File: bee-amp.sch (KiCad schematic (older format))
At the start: 35 parts, among them J1 Conn_01x02_Male, J10 Conn_01x02, J2 Conn_01x02_Male, J3 Conn_01x02_Male, J4 Conn_01x02_Male, J7 Conn_01x03, J8 Conn_01x02, J9 Conn_01x02, U1 OP07

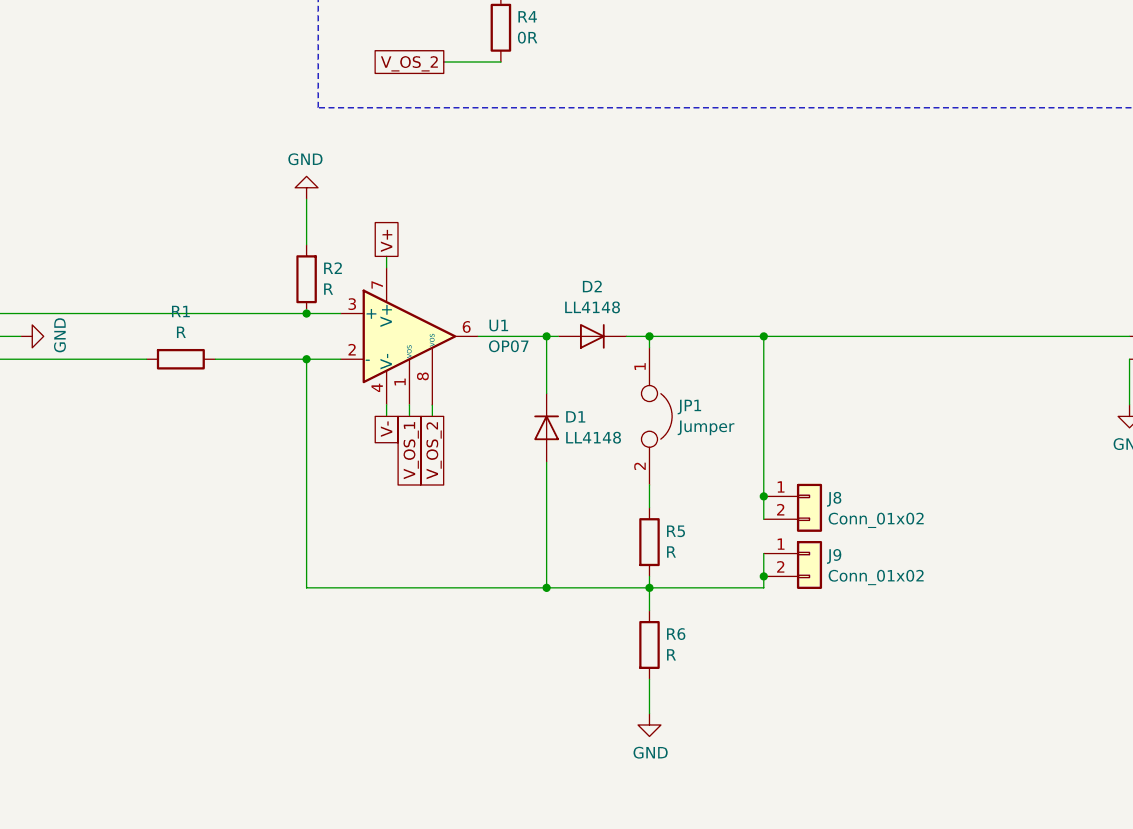
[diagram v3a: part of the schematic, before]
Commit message: Add part values, numbers and placement variants.
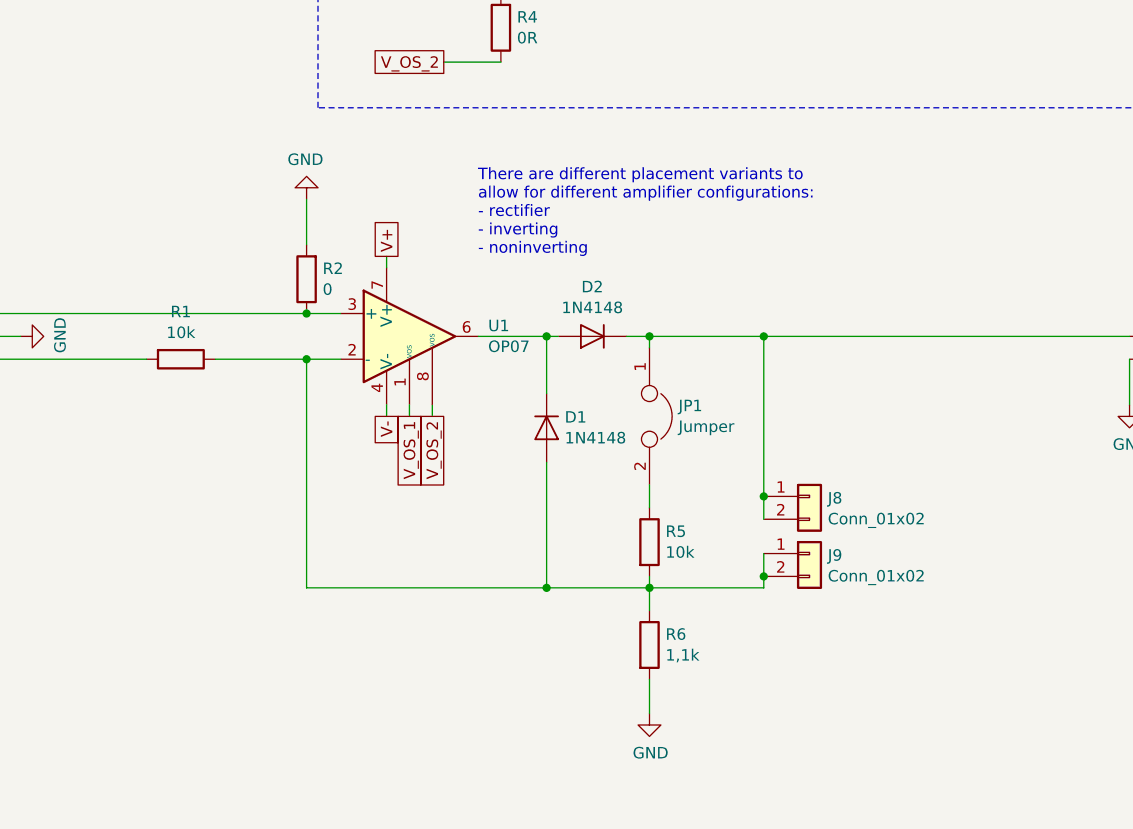
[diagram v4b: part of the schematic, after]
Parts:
- C1, C2: Reichelt Part No (none) -> X7R-G0805 100N; order number KEM X7R0805 100N -> (none)
- D1, D2: value LL4148 -> 1N4148; Reichelt Part No (none) -> 1N 4148 SMD; fit_field (none) -> +rectifier; order number 1N 4148 SMD -> (none)
- J1, J10, J2, J3, J4, JP1: Reichelt Part No (none) -> RND 205-00623
- J7: Reichelt Part No (none) -> RND 205-00624
- J8, J9: Reichelt Part No (none) -> MPE 006-1-002
- R1: value R -> 10k; Reichelt Part No (none) -> SMD-0805 10,0K; fit_field (none) -> +rectifier,+inverting
- R2: value R -> 0; Reichelt Part No (none) -> SMD-0805 0,00; fit_field (none) -> +rectifier,+inverting
- R3, R4: Reichelt Part No (none) -> RND 0805 1 0
- R5: value R -> 10k; Reichelt Part No (none) -> SMD-0805 10,0K
- R6: value R -> 1,1k; Reichelt Part No (none) -> RND 0805 1 1,1K; fit_field (none) -> +noninverting
- RV1: Reichelt Part No (none) -> 23A-20K; order number 23A-20K -> (none)
- U1: Reichelt Part No (none) -> OP 07 CD; order number OP 07 CD -> (none)
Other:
- note added: "There are different placement variants to \nallow for different amplifier configurations:\n- rectifier\n- inverting\n- noninverting"
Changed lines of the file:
@@
 F 2 "Connector_PinHeader_2.54mm:PinHeader_1x02_P2.54mm_Vertical" H 850 1300 50  0001 C CNN
 F 3 "~" H 850 1300 50  0001 C CNN
+F 4 "RND 205-00623" H 850 1300 50  0001 C CNN "Reichelt Part No"
 	1    850  1300
 	1    0    0    -1
@@
 F 2 "Connector_PinHeader_2.54mm:PinHeader_1x02_P2.54mm_Vertical" H 850 950 50  0001 C CNN
 F 3 "~" H 850 950 50  0001 C CNN
+F 4 "RND 205-00623" H 850 950 50  0001 C CNN "Reichelt Part No"
 	1    850  950
 	1    0    0    -1
@@
 F 2 "Connector_PinHeader_2.54mm:PinHeader_1x02_P2.54mm_Vertical" H 850 2150 50  0001 C CNN
 F 3 "~" H 850 2150 50  0001 C CNN
+F 4 "RND 205-00623" H 850 2150 50  0001 C CNN "Reichelt Part No"
 	1    850  2150
 	1    0    0    -1
@@
 F 2 "Connector_PinHeader_2.54mm:PinHeader_1x02_P2.54mm_Vertical" H 850 1800 50  0001 C CNN
 F 3 "~" H 850 1800 50  0001 C CNN
+F 4 "RND 205-00623" H 850 1800 50  0001 C CNN "Reichelt Part No"
 	1    850  1800
 	1    0    0    -1
@@
 F 2 "Package_SO:SO-8_5.3x6.2mm_P1.27mm" H 5550 3650 50  0001 C CNN
 F 3 "https://www.analog.com/media/en/technical-documentation/data-sheets/OP07.pdf" H 5550 3750 50  0001 C CNN
-F 4 "OP 07 CD" H 5500 3600 50  0001 C CNN "order number"
+F 4 "OP 07 CD" H 5500 3600 50  0001 C CNN "Reichelt Part No"
 	1    5500 3600
 	1    0    0    -1
@@
 F 2 "Connector_PinHeader_2.54mm:PinHeader_1x03_P2.54mm_Vertical" H 3400 3600 50  0001 C CNN
 F 3 "~" H 3400 3600 50  0001 C CNN
+F 4 "RND 205-00624" H 3400 3600 50  0001 C CNN "Reichelt Part No"
 	1    3400 3600
 	-1   0    0    -1
@@
 F 2 "Connector_PinHeader_2.54mm:PinHeader_1x02_P2.54mm_Vertical" H 8850 3600 50  0001 C CNN
 F 3 "~" H 8850 3600 50  0001 C CNN
+F 4 "RND 205-00623" H 8850 3600 50  0001 C CNN "Reichelt Part No"
 	1    8850 3600
 	1    0    0    -1
@@
 F 2 "Capacitor_SMD:C_0805_2012Metric_Pad1.15x1.40mm_HandSolder" H 2638 1050 50  0001 C CNN
 F 3 "https://www.reichelt.de/index.html?ACTION=7&LA=3&OPEN=0&INDEX=0&FILENAME=B300%252FKEM_C0XXX_X7R_DB-EN.pdf" H 2600 1200 50  0001 C CNN
-F 4 "KEM X7R0805 100N" H 2600 1200 50  0001 C CNN "order number"
+F 4 "X7R-G0805 100N" H 2600 1200 50  0001 C CNN "Reichelt Part No"
 	1    2600 1200
 	1    0    0    -1
@@
 P 4500 3700
 F 0 "R1" V 4293 3700 50  0000 C CNN
-F 1 "R" V 4384 3700 50  0000 C CNN
+F 1 "10k" V 4384 3700 50  0000 C CNN
 F 2 "Resistor_SMD:R_0805_2012Metric_Pad1.15x1.40mm_HandSolder" V 4430 3700 50  0001 C CNN
 F 3 "~" H 4500 3700 50  0001 C CNN
+F 4 "SMD-0805 10,0K" H 4500 3700 50  0001 C CNN "Reichelt Part No"
+F 5 "+rectifier,+inverting" H 4500 3700 50  0001 C CNN "fit_field"
 	1    4500 3700
 	0    1    1    0
@@
 P 6300 3600
 F 0 "D2" H 6300 3384 50  0000 C CNN
-F 1 "LL4148" H 6300 3475 50  0000 C CNN
+F 1 "1N4148" H 6300 3475 50  0000 C CNN
 F 2 "Diode_SMD:D_MiniMELF" H 6300 3425 50  0001 C CNN
 F 3 "http://www.vishay.com/docs/85557/ll4148.pdf" H 6300 3600 50  0001 C CNN
-F 4 "1N 4148 SMD" H 6300 3600 50  0001 C CNN "order number"
+F 4 "1N 4148 SMD" H 6300 3600 50  0001 C CNN "Reichelt Part No"
+F 5 "+rectifier" H 6300 3600 50  0001 C CNN "fit_field"
 	1    6300 3600
 	-1   0    0    1
@@
 F 2 "Capacitor_SMD:C_0805_2012Metric_Pad1.15x1.40mm_HandSolder" H 3688 1050 50  0001 C CNN
 F 3 "https://www.reichelt.de/index.html?ACTION=7&LA=3&OPEN=0&INDEX=0&FILENAME=B300%252FKEM_C0XXX_X7R_DB-EN.pdf" H 3650 1200 50  0001 C CNN
-F 4 "KEM X7R0805 100N" H 3650 1200 50  0001 C CNN "order number"
+F 4 "X7R-G0805 100N" H 3650 1200 50  0001 C CNN "Reichelt Part No"
 	1    3650 1200
 	1    0    0    -1
@@
 P 6550 4500
 F 0 "R5" H 6620 4546 50  0000 L CNN
-F 1 "R" H 6620 4455 50  0000 L CNN
+F 1 "10k" H 6620 4455 50  0000 L CNN
 F 2 "Resistor_SMD:R_0805_2012Metric_Pad1.15x1.40mm_HandSolder" V 6480 4500 50  0001 C CNN
 F 3 "~" H 6550 4500 50  0001 C CNN
+F 4 "SMD-0805 10,0K" H 6550 4500 50  0001 C CNN "Reichelt Part No"
 	1    6550 4500
 	1    0    0    -1
@@
 P 6550 4950
 F 0 "R6" H 6620 4996 50  0000 L CNN
-F 1 "R" H 6620 4905 50  0000 L CNN
+F 1 "1,1k" H 6620 4905 50  0000 L CNN
 F 2 "Resistor_SMD:R_0805_2012Metric_Pad1.15x1.40mm_HandSolder" V 6480 4950 50  0001 C CNN
 F 3 "~" H 6550 4950 50  0001 C CNN
+F 4 "RND 0805 1 1,1K" H 6550 4950 50  0001 C CNN "Reichelt Part No"
+F 5 "+noninverting" H 6550 4950 50  0001 C CNN "fit_field"
 	1    6550 4950
 	1    0    0    -1
@@
 P 6100 4000
 F 0 "D1" V 6054 4079 50  0000 L CNN
-F 1 "LL4148" V 6145 4079 50  0000 L CNN
+F 1 "1N4148" V 6145 4079 50  0000 L CNN
 F 2 "Diode_SMD:D_MiniMELF" H 6100 3825 50  0001 C CNN
 F 3 "http://www.vishay.com/docs/85557/ll4148.pdf" H 6100 4000 50  0001 C CNN
-F 4 "1N 4148 SMD" H 6100 4000 50  0001 C CNN "order number"
+F 4 "1N 4148 SMD" H 6100 4000 50  0001 C CNN "Reichelt Part No"
+F 5 "+rectifier" H 6100 4000 50  0001 C CNN "fit_field"
 	1    6100 4000
 	0    1    1    0
@@
 P 5050 3350
 F 0 "R2" H 4980 3304 50  0000 R CNN
-F 1 "R" H 4980 3395 50  0000 R CNN
+F 1 "0" H 4980 3395 50  0000 R CNN
 F 2 "Resistor_SMD:R_0805_2012Metric_Pad1.15x1.40mm_HandSolder" V 4980 3350 50  0001 C CNN
 F 3 "~" H 5050 3350 50  0001 C CNN
+F 4 "SMD-0805 0,00" H 5050 3350 50  0001 C CNN "Reichelt Part No"
+F 5 "+rectifier,+inverting" H 5050 3350 50  0001 C CNN "fit_field"
 	1    5050 3350
 	-1   0    0    1
@@
 F 2 "Connector_PinSocket_2.54mm:PinSocket_1x02_P2.54mm_Vertical" H 7250 4300 50  0001 C CNN
 F 3 "~" H 7250 4300 50  0001 C CNN
+F 4 "MPE 006-1-002" H 7250 4300 50  0001 C CNN "Reichelt Part No"
 	1    7250 4300
 	1    0    0    -1
@@
 F 2 "Connector_PinSocket_2.54mm:PinSocket_1x02_P2.54mm_Vertical" H 7250 4550 50  0001 C CNN
 F 3 "~" H 7250 4550 50  0001 C CNN
+F 4 "MPE 006-1-002" H 7250 4550 50  0001 C CNN "Reichelt Part No"
 	1    7250 4550
 	1    0    0    -1
@@
 F 2 "Connector_PinHeader_2.54mm:PinHeader_1x02_P2.54mm_Vertical" H 6550 3950 50  0001 C CNN
 F 3 "~" H 6550 3950 50  0001 C CNN
+F 4 "RND 205-00623" H 6550 3950 50  0001 C CNN "Reichelt Part No"
 	1    6550 3950
 	0    1    1    0
@@
 F 2 "Potentiometer_SMD:Potentiometer_Bourns_3314J_Vertical" H 5900 1850 50  0001 C CNN
 F 3 "https://cdn-reichelt.de/documents/datenblatt/B400/BI-SERIE-23.pdf" H 5900 1850 50  0001 C CNN
-F 4 "23A-20K" H 5900 1850 50  0001 C CNN "order number"
+F 4 "23A-20K" H 5900 1850 50  0001 C CNN "Reichelt Part No"
 	1    5900 1850
 	1    0    0    -1
@@
 F 2 "Resistor_SMD:R_0805_2012Metric_Pad1.15x1.40mm_HandSolder" V 5830 1450 50  0001 C CNN
 F 3 "~" H 5900 1450 50  0001 C CNN
+F 4 "RND 0805 1 0" H 5900 1450 50  0001 C CNN "Reichelt Part No"
 	1    5900 1450
 	-1   0    0    1
@@
 F 2 "Resistor_SMD:R_0805_2012Metric_Pad1.15x1.40mm_HandSolder" V 5830 2250 50  0001 C CNN
 F 3 "~" H 5900 2250 50  0001 C CNN
+F 4 "RND 0805 1 0" H 5900 2250 50  0001 C CNN "Reichelt Part No"
 	1    5900 2250
 	-1   0    0    1
@@
 	1    0    0    -1
 $EndComp
+Text Notes 5800 3250 0    50   ~ 0
+There are different placement variants to \nallow for different amplifier configurations:\n- rectifier\n- inverting\n- noninverting
 $EndSCHEMATC

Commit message: Unify part numbers.
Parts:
- R2: Reichelt Part No SMD-0805 0,00 -> RND 0805 1 0
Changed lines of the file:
@@
 F 2 "Resistor_SMD:R_0805_2012Metric_Pad1.15x1.40mm_HandSolder" V 4980 3350 50  0001 C CNN
 F 3 "~" H 5050 3350 50  0001 C CNN
-F 4 "SMD-0805 0,00" H 5050 3350 50  0001 C CNN "Reichelt Part No"
+F 4 "RND 0805 1 0" H 5050 3350 50  0001 C CNN "Reichelt Part No"
 F 5 "+rectifier,+inverting" H 5050 3350 50  0001 C CNN "fit_field"
 	1    5050 3350

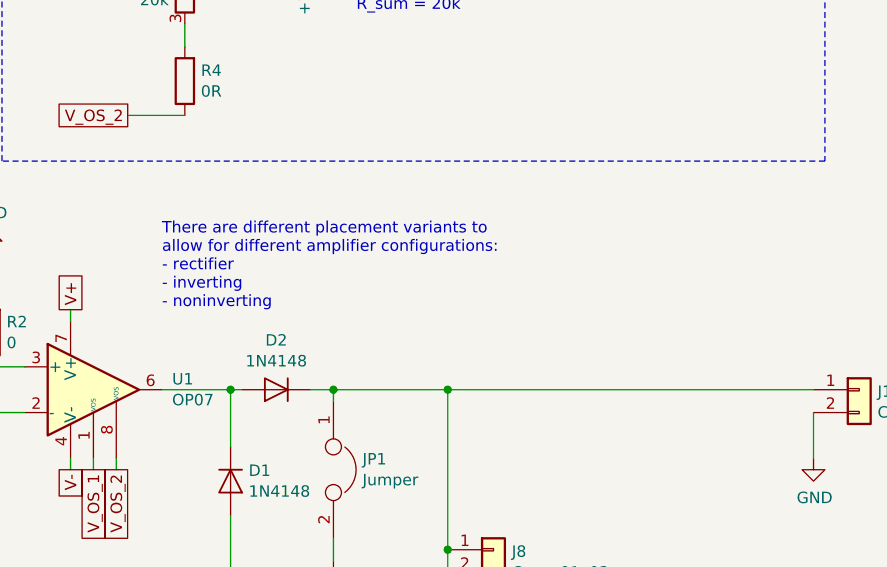
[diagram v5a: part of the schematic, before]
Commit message: Update info on placement variants.
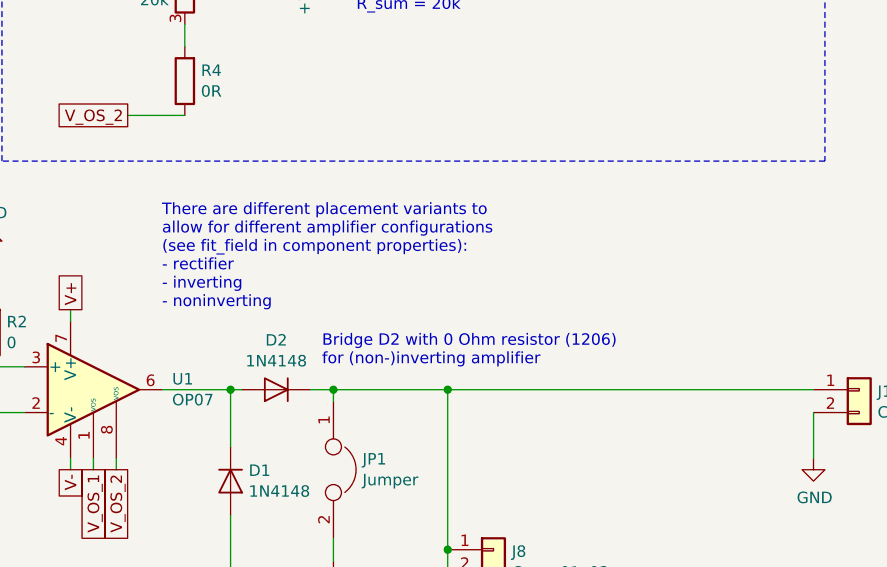
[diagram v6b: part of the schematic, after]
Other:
- note added: "Bridge D2 with 0 Ohm resistor (1206)\nfor (non-)inverting amplifier"
- note added: "There are different placement variants to \nallow for different amplifier configurations\n(see fit_field in component properties):\n- rectifier\n- inverting\n- noninverting"
- note removed: "There are different placement variants to \nallow for different amplifier configurations:\n- rectifier\n- inverting\n- noninverting"
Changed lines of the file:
@@
 $EndComp
 Text Notes 5800 3250 0    50   ~ 0
-There are different placement variants to \nallow for different amplifier configurations:\n- rectifier\n- inverting\n- noninverting
+There are different placement variants to \nallow for different amplifier configurations\n(see fit_field in component properties):\n- rectifier\n- inverting\n- noninverting
+Text Notes 6500 3500 0    50   ~ 0
+Bridge D2 with 0 Ohm resistor (1206)\nfor (non-)inverting amplifier
 $EndSCHEMATC

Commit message: Replace SO package by SOIC. Fixes #1.
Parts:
- U1: footprint Package_SO:SO-8_5.3x6.2mm_P1.27mm -> Package_SO:SOIC-8_3.9x4.9mm_P1.27mm
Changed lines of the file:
@@
 F 0 "U1" H 5844 3646 50  0000 L CNN
 F 1 "OP07" H 5844 3555 50  0000 L CNN
-F 2 "Package_SO:SO-8_5.3x6.2mm_P1.27mm" H 5550 3650 50  0001 C CNN
+F 2 "Package_SO:SOIC-8_3.9x4.9mm_P1.27mm" H 5550 3650 50  0001 C CNN
 F 3 "https://www.analog.com/media/en/technical-documentation/data-sheets/OP07.pdf" H 5550 3750 50  0001 C CNN
 F 4 "OP 07 CD" H 5500 3600 50  0001 C CNN "Reichelt Part No"

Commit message: Relabel as bee specific.
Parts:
- H1, H2: footprint Symbol-emt:Text_U_B+_Silkscreen -> Symbol-bee:Text_U_B+_Silkscreen; symbol Mechanical-emt:Silkscreen_Label -> Mechanical-bee:Silkscreen_Label
- H13: footprint Symbol-emt:EMT-Logo_5.1x2.5mm_Silkscreen -> Symbol-bee:EMT-Logo_5.1x2.5mm_Silkscreen; symbol Mechanical-emt:Silkscreen_Label -> Mechanical-bee:Silkscreen_Label
- H14: footprint Symbol-emt:BEE-Logo_Silkscreen_small -> Symbol-bee:BEE-Logo_Silkscreen_small; symbol Mechanical-emt:Silkscreen_Label -> Mechanical-bee:Silkscreen_Label
- H3, H4: footprint Symbol-emt:Text_U_B-_Silkscreen -> Symbol-bee:Text_U_B-_Silkscreen; symbol Mechanical-emt:Silkscreen_Label -> Mechanical-bee:Silkscreen_Label
- H5, H6: footprint Symbol-emt:Text_U_B2_Silkscreen -> Symbol-bee:Text_U_B2_Silkscreen; symbol Mechanical-emt:Silkscreen_Label -> Mechanical-bee:Silkscreen_Label
- H7, H8: footprint Symbol-emt:Symbol_GND_Silkscreen -> Symbol-bee:Symbol_GND_Silkscreen; symbol Mechanical-emt:Silkscreen_Label -> Mechanical-bee:Silkscreen_Label
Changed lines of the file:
@@
 	5650 1300 5900 1300
 $Comp
-L Mechanical-emt:Silkscreen_Label H1
+L Mechanical-bee:Silkscreen_Label H1
 U 1 1 5CCC8957
 P 1050 6600
 F 0 "H1" H 1175 6645 50  0000 L CNN
 F 1 "Silkscreen_Label" H 1175 6554 50  0000 L CNN
-F 2 "Symbol-emt:Text_U_B+_Silkscreen" H 1050 6600 50  0001 C CNN
+F 2 "Symbol-bee:Text_U_B+_Silkscreen" H 1050 6600 50  0001 C CNN
 F 3 "~" H 1050 6600 50  0001 C CNN
 	1    1050 6600
@@
 $EndComp
 $Comp
-L Mechanical-emt:Silkscreen_Label H2
+L Mechanical-bee:Silkscreen_Label H2
 U 1 1 5CCC93D9
 P 1050 6800
 F 0 "H2" H 1175 6845 50  0000 L CNN
 F 1 "Silkscreen_Label" H 1175 6754 50  0000 L CNN
-F 2 "Symbol-emt:Text_U_B+_Silkscreen" H 1050 6800 50  0001 C CNN
+F 2 "Symbol-bee:Text_U_B+_Silkscreen" H 1050 6800 50  0001 C CNN
 F 3 "~" H 1050 6800 50  0001 C CNN
 	1    1050 6800
@@
 $EndComp
 $Comp
-L Mechanical-emt:Silkscreen_Label H3
+L Mechanical-bee:Silkscreen_Label H3
 U 1 1 5CCCAC57
 P 1050 7000
 F 0 "H3" H 1175 7045 50  0000 L CNN
 F 1 "Silkscreen_Label" H 1175 6954 50  0000 L CNN
-F 2 "Symbol-emt:Text_U_B-_Silkscreen" H 1050 7000 50  0001 C CNN
+F 2 "Symbol-bee:Text_U_B-_Silkscreen" H 1050 7000 50  0001 C CNN
 F 3 "~" H 1050 7000 50  0001 C CNN
 	1    1050 7000
@@
 $EndComp
 $Comp
-L Mechanical-emt:Silkscreen_Label H4
+L Mechanical-bee:Silkscreen_Label H4
 U 1 1 5CCCAF9B
 P 1050 7200
 F 0 "H4" H 1175 7245 50  0000 L CNN
 F 1 "Silkscreen_Label" H 1175 7154 50  0000 L CNN
-F 2 "Symbol-emt:Text_U_B-_Silkscreen" H 1050 7200 50  0001 C CNN
+F 2 "Symbol-bee:Text_U_B-_Silkscreen" H 1050 7200 50  0001 C CNN
 F 3 "~" H 1050 7200 50  0001 C CNN
 	1    1050 7200
@@
 $EndComp
 $Comp
-L Mechanical-emt:Silkscreen_Label H5
+L Mechanical-bee:Silkscreen_Label H5
 U 1 1 5CCCB104
 P 1950 6600
 F 0 "H5" H 2075 6645 50  0000 L CNN
 F 1 "Silkscreen_Label" H 2075 6554 50  0000 L CNN
-F 2 "Symbol-emt:Text_U_B2_Silkscreen" H 1950 6600 50  0001 C CNN
+F 2 "Symbol-bee:Text_U_B2_Silkscreen" H 1950 6600 50  0001 C CNN
 F 3 "~" H 1950 6600 50  0001 C CNN
 	1    1950 6600
@@
 $EndComp
 $Comp
-L Mechanical-emt:Silkscreen_Label H6
+L Mechanical-bee:Silkscreen_Label H6
 U 1 1 5CCCB407
 P 1950 6800
 F 0 "H6" H 2075 6845 50  0000 L CNN
 F 1 "Silkscreen_Label" H 2075 6754 50  0000 L CNN
-F 2 "Symbol-emt:Text_U_B2_Silkscreen" H 1950 6800 50  0001 C CNN
+F 2 "Symbol-bee:Text_U_B2_Silkscreen" H 1950 6800 50  0001 C CNN
 F 3 "~" H 1950 6800 50  0001 C CNN
 	1    1950 6800
@@
 $EndComp
 $Comp
-L Mechanical-emt:Silkscreen_Label H7
+L Mechanical-bee:Silkscreen_Label H7
 U 1 1 5CCCB63D
 P 1950 7000
 F 0 "H7" H 2075 7045 50  0000 L CNN
 F 1 "Silkscreen_Label" H 2075 6954 50  0000 L CNN
-F 2 "Symbol-emt:Symbol_GND_Silkscreen" H 1950 7000 50  0001 C CNN
+F 2 "Symbol-bee:Symbol_GND_Silkscreen" H 1950 7000 50  0001 C CNN
 F 3 "~" H 1950 7000 50  0001 C CNN
 	1    1950 7000
@@
 $EndComp
 $Comp
-L Mechanical-emt:Silkscreen_Label H8
+L Mechanical-bee:Silkscreen_Label H8
 U 1 1 5CCCB8AF
 P 1950 7200
 F 0 "H8" H 2075 7245 50  0000 L CNN
 F 1 "Silkscreen_Label" H 2075 7154 50  0000 L CNN
-F 2 "Symbol-emt:Symbol_GND_Silkscreen" H 1950 7200 50  0001 C CNN
+F 2 "Symbol-bee:Symbol_GND_Silkscreen" H 1950 7200 50  0001 C CNN
 F 3 "~" H 1950 7200 50  0001 C CNN
 	1    1950 7200
@@
 $EndComp
 $Comp
-L Mechanical-emt:Silkscreen_Label H13
+L Mechanical-bee:Silkscreen_Label H13
 U 1 1 5CCCB2BD
 P 1050 7400
 F 0 "H13" H 1175 7445 50  0000 L CNN
 F 1 "Silkscreen_Label" H 1175 7354 50  0000 L CNN
-F 2 "Symbol-emt:EMT-Logo_5.1x2.5mm_Silkscreen" H 1050 7400 50  0001 C CNN
+F 2 "Symbol-bee:EMT-Logo_5.1x2.5mm_Silkscreen" H 1050 7400 50  0001 C CNN
 F 3 "~" H 1050 7400 50  0001 C CNN
 	1    1050 7400
@@
 $EndComp
 $Comp
-L Mechanical-emt:Silkscreen_Label H14
+L Mechanical-bee:Silkscreen_Label H14
 U 1 1 5CCCB365
 P 1950 7400
 F 0 "H14" H 2075 7445 50  0000 L CNN
 F 1 "Silkscreen_Label" H 2075 7354 50  0000 L CNN
-F 2 "Symbol-emt:BEE-Logo_Silkscreen_small" H 1950 7400 50  0001 C CNN
+F 2 "Symbol-bee:BEE-Logo_Silkscreen_small" H 1950 7400 50  0001 C CNN
 F 3 "~" H 1950 7400 50  0001 C CNN
 	1    1950 7400
